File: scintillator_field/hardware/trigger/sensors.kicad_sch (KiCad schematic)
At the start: 28 parts

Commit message: conclude schematic
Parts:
- C10: renamed from C22; footprint Capacitor_SMD:C_0805_2012Metric_Pad1.18x1.45mm_HandSolder -> Capacitor_SMD:C_0402_1005Metric
- C11: renamed from C23; footprint Capacitor_SMD:C_0805_2012Metric_Pad1.18x1.45mm_HandSolder -> Capacitor_SMD:C_0402_1005Metric
- C12: renamed from C24; footprint Capacitor_SMD:C_0805_2012Metric_Pad1.18x1.45mm_HandSolder -> Capacitor_SMD:C_0402_1005Metric
- C13: renamed from C25; footprint Capacitor_SMD:C_0805_2012Metric_Pad1.18x1.45mm_HandSolder -> Capacitor_SMD:C_0402_1005Metric
- C14: renamed from C26; footprint Capacitor_SMD:C_0805_2012Metric_Pad1.18x1.45mm_HandSolder -> Capacitor_SMD:C_0402_1005Metric
- C15: renamed from C27; footprint Capacitor_SMD:C_0805_2012Metric_Pad1.18x1.45mm_HandSolder -> Capacitor_SMD:C_0402_1005Metric
- C16: renamed from C28; footprint Capacitor_SMD:C_0805_2012Metric_Pad1.18x1.45mm_HandSolder -> Capacitor_SMD:C_0402_1005Metric
- C17: renamed from C29; footprint Capacitor_SMD:C_0805_2012Metric_Pad1.18x1.45mm_HandSolder -> Capacitor_SMD:C_0402_1005Metric
- C18: renamed from C30; footprint Capacitor_SMD:C_0805_2012Metric_Pad1.18x1.45mm_HandSolder -> Capacitor_SMD:C_0402_1005Metric
- C19: renamed from C31; footprint Capacitor_SMD:C_0805_2012Metric_Pad1.18x1.45mm_HandSolder -> Capacitor_SMD:C_0402_1005Metric
- C20: renamed from C32; footprint Capacitor_SMD:C_0805_2012Metric_Pad1.18x1.45mm_HandSolder -> Capacitor_SMD:C_0402_1005Metric
- C21: renamed from C33; footprint Capacitor_SMD:C_0805_2012Metric_Pad1.18x1.45mm_HandSolder -> Capacitor_SMD:C_0402_1005Metric
- C22: renamed from C34; footprint Capacitor_SMD:C_0805_2012Metric_Pad1.18x1.45mm_HandSolder -> Capacitor_SMD:C_0402_1005Metric
- C23: renamed from C35; footprint Capacitor_SMD:C_0805_2012Metric_Pad1.18x1.45mm_HandSolder -> Capacitor_SMD:C_0402_1005Metric
- C24: renamed from C36; footprint Capacitor_SMD:C_0805_2012Metric_Pad1.18x1.45mm_HandSolder -> Capacitor_SMD:C_0402_1005Metric
- C9: renamed from C21; footprint Capacitor_SMD:C_0805_2012Metric_Pad1.18x1.45mm_HandSolder -> Capacitor_SMD:C_0402_1005Metric
- renumbered D4 to D3, D5 to D4, R12 to R11, R8 to R12, R9 to R14, R14 to R15, R10 to R16, R15 to R17, R11 to R18

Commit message: pcb v1
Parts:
- R11, R12, R13, R14, R15, R16, R17, R18: footprint Resistor_SMD:R_0805_2012Metric_Pad1.20x1.40mm_HandSolder -> Resistor_SMD:R_0402_1005Metric
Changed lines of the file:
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@@
 			)
 		)
-		(property "Footprint" "Resistor_SMD:R_0805_2012Metric_Pad1.20x1.40mm_HandSolder"
+		(property "Footprint" "Resistor_SMD:R_0402_1005Metric"
 			(at 80.01 86.868 90)
 			(effects
@@
 			)
 		)
-		(property "Footprint" "Resistor_SMD:R_0805_2012Metric_Pad1.20x1.40mm_HandSolder"
+		(property "Footprint" "Resistor_SMD:R_0402_1005Metric"
 			(at 80.01 116.078 90)
 			(effects
@@
 			)
 		)
-		(property "Footprint" "Resistor_SMD:R_0805_2012Metric_Pad1.20x1.40mm_HandSolder"
+		(property "Footprint" "Resistor_SMD:R_0402_1005Metric"
 			(at 106.68 57.658 90)
 			(effects
@@
 			)
 		)
-		(property "Footprint" "Resistor_SMD:R_0805_2012Metric_Pad1.20x1.40mm_HandSolder"
+		(property "Footprint" "Resistor_SMD:R_0402_1005Metric"
 			(at 106.68 145.288 90)
 			(effects
@@
 			)
 		)
-		(property "Footprint" "Resistor_SMD:R_0805_2012Metric_Pad1.20x1.40mm_HandSolder"
+		(property "Footprint" "Resistor_SMD:R_0402_1005Metric"
 			(at 106.68 116.078 90)
 			(effects
@@
 			)
 		)
-		(property "Footprint" "Resistor_SMD:R_0805_2012Metric_Pad1.20x1.40mm_HandSolder"
+		(property "Footprint" "Resistor_SMD:R_0402_1005Metric"
 			(at 80.01 57.658 90)
 			(effects
@@
 			)
 		)
-		(property "Footprint" "Resistor_SMD:R_0805_2012Metric_Pad1.20x1.40mm_HandSolder"
+		(property "Footprint" "Resistor_SMD:R_0402_1005Metric"
 			(at 80.01 145.288 90)
 			(effects
@@
 			)
 		)
-		(property "Footprint" "Resistor_SMD:R_0805_2012Metric_Pad1.20x1.40mm_HandSolder"
+		(property "Footprint" "Resistor_SMD:R_0402_1005Metric"
 			(at 106.68 86.868 90)
 			(effects

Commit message: pcb fabrication files
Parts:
- C10, C11, C12, C13, C14, C15, C16, C17, C18, C19, C20, C21, C22, C23, C24, C9: LCSC (none) -> C1524
- R11, R12, R13, R14, R15, R16, R17, R18: LCSC (none) -> C25120

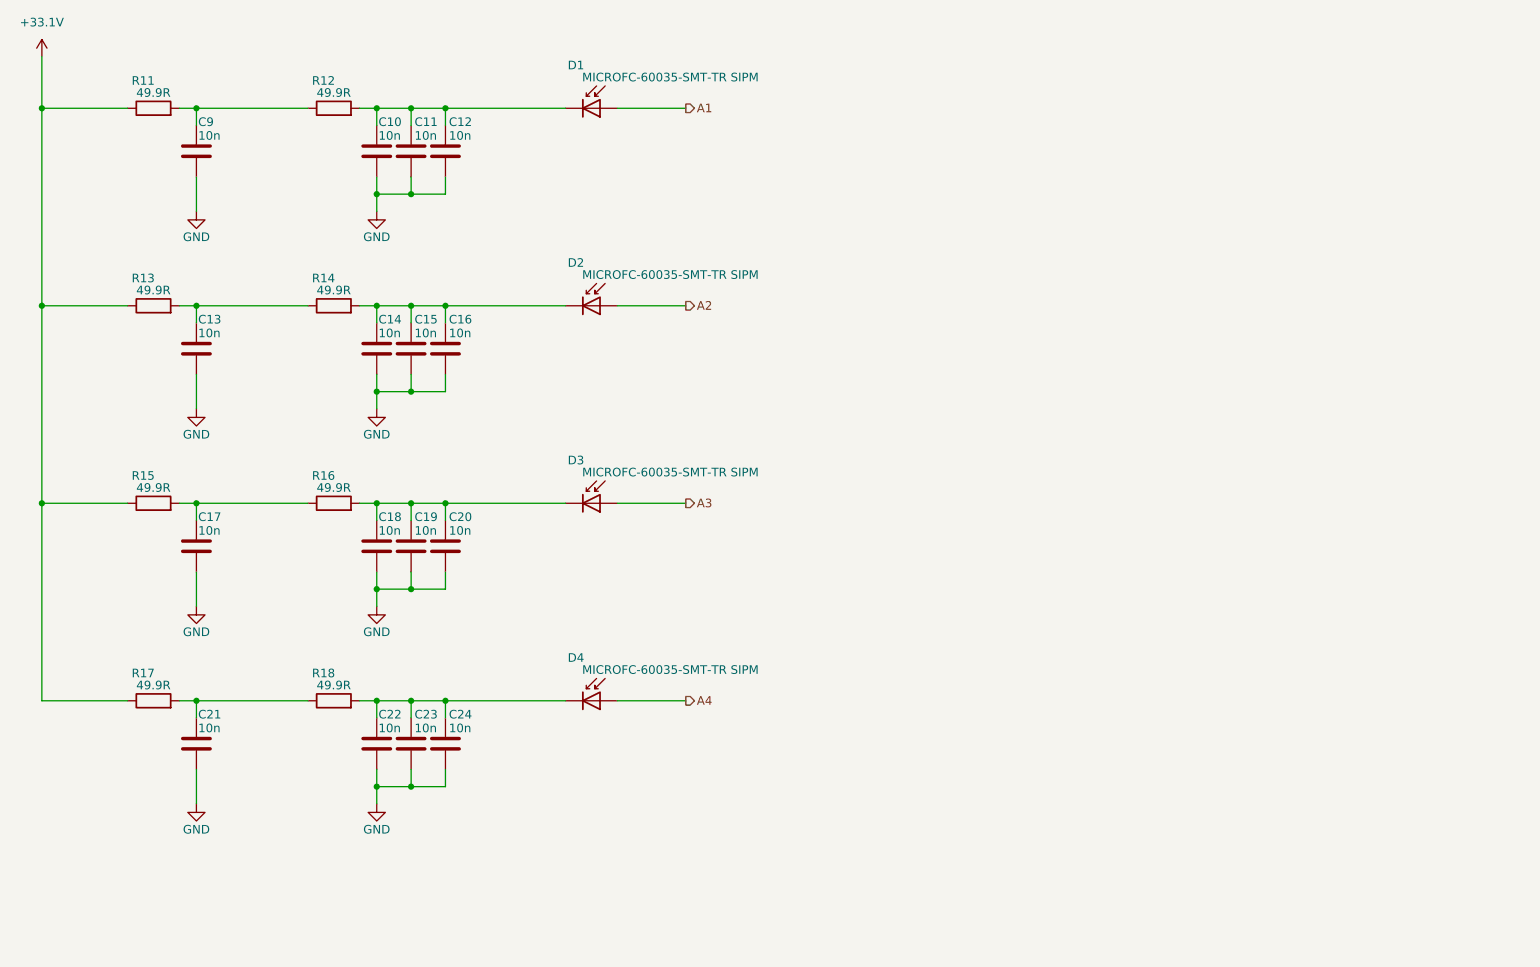
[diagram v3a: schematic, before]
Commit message: update to opa858
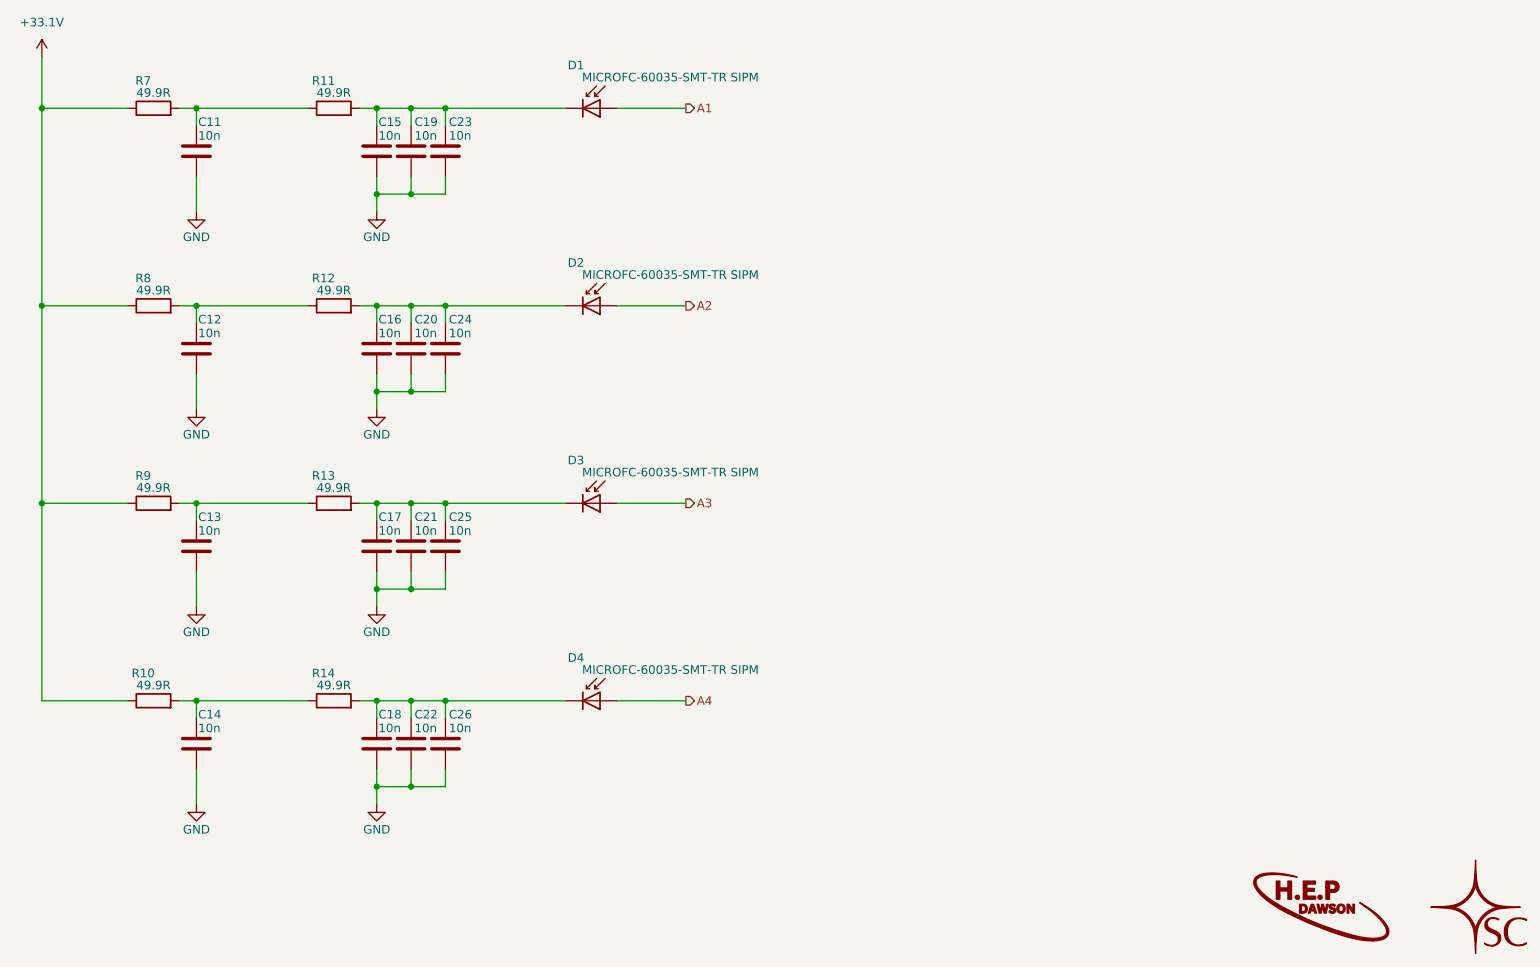
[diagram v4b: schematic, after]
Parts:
- renumbered C9 to C11, C13 to C12, C17 to C13, C21 to C14, C10 to C15, C14 to C16, C18 to C17, C22 to C18, C11 to C19, C15 to C20, C19 to C21, C23 to C22, C12 to C23, C16 to C24, C20 to C25, C24 to C26, R17 to R10, R12 to R11, R14 to R12, R16 to R13, R18 to R14, R11 to R7, R13 to R8, R15 to R9
